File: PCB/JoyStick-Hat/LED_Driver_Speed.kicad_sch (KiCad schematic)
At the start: 0 parts

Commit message: Power and LED Driver
Power Supply Schematic sketched out using Pololu power regulator modules to hasten design. LED drivers replaced with ones that have 24 ouputs so we can use 20 unit bar graph LEDs and have 8 extra channels for other onboard LEDs
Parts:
- added J1: Conn_02x10_Counter_Clockwise, Connector_PinHeader_2.54mm:PinHeader_2x10_P2.54mm_Vertical, symbol Connector_Generic:Conn_02x10_Counter_Clockwise
- added U2: TLC5947DAP, AVR-KiCAD-Lib-ICs:DAP32_4P36X4P11, symbol AVR-KiCAD-Lib-ICs:TLC5947DAP
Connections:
- new net: J1.5 (Pin_5), U2.10 (OUT5)
- new net: J1.6 (Pin_6), U2.11 (OUT6)
- new net: J1.7 (Pin_7), U2.12 (OUT7)
- new net: J1.8 (Pin_8), U2.13 (OUT8)
- new net: J1.9 (Pin_9), U2.14 (OUT9)
- new net: J1.10 (Pin_10), U2.15 (OUT10)
- new net: J1.11 (Pin_11), U2.16 (OUT11)
- new net: J1.12 (Pin_12), U2.17 (OUT12)
- new net: J1.13 (Pin_13), U2.18 (OUT13)
- new net: J1.14 (Pin_14), U2.19 (OUT14)
- new net: J1.15 (Pin_15), U2.20 (OUT15)
- new net: J1.16 (Pin_16), U2.21 (OUT16)
- new net: J1.17 (Pin_17), U2.22 (OUT17)
- new net: J1.18 (Pin_18), U2.23 (OUT18)
- new net: J1.19 (Pin_19), U2.24 (OUT19)
- new net: J1.20 (Pin_20), U2.25 (OUT20)
- new net: J1.1 (Pin_1), U2.6 (OUT1)
- new net: J1.2 (Pin_2), U2.7 (OUT2)
- new net: J1.3 (Pin_3), U2.8 (OUT3)
- new net: J1.4 (Pin_4), U2.9 (OUT4)
- new net GND: U2.1 (GND), U2.33 (GND_PAD)

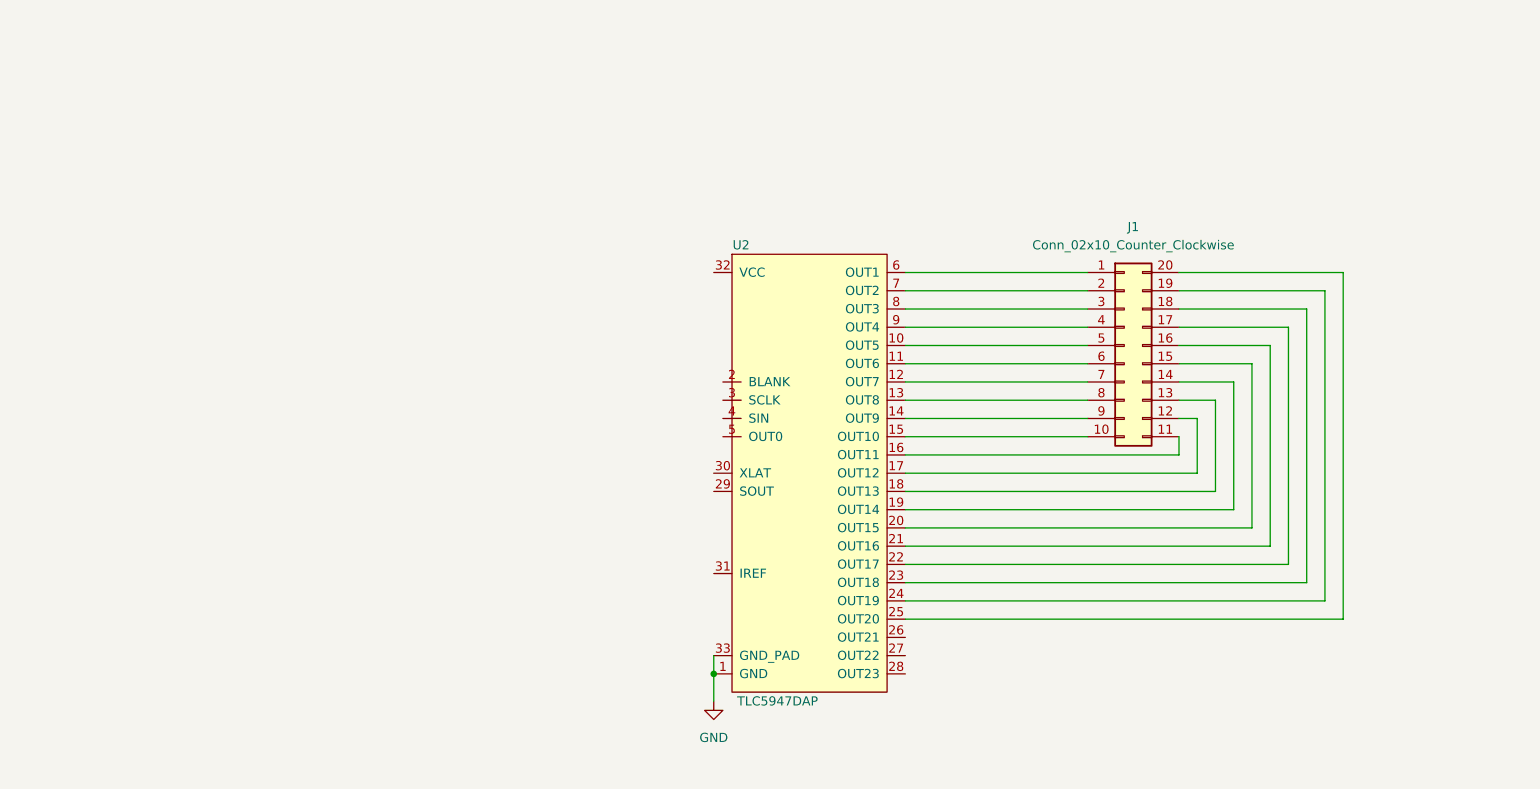
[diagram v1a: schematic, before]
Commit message: LED drivers and Joystick
Finished LED driver scheamtics, corrected some problems with symbols. added conenctors for joystick and buttons, connected RPI pins to MCU
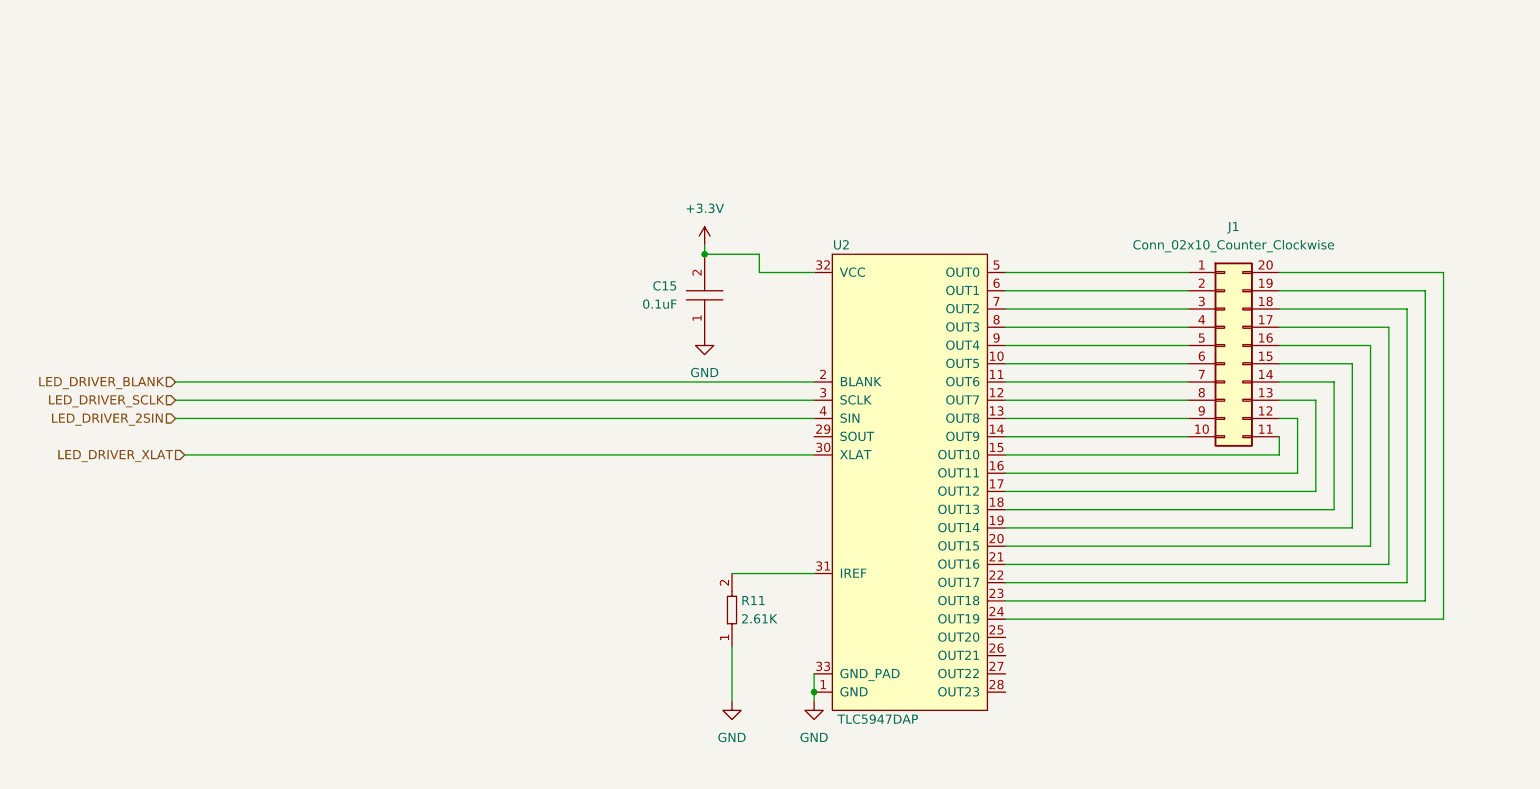
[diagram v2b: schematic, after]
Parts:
- added C15: CL10B104JB8NNNC, AVR-KiCAD-Lib-Capacitors:C0603, symbol AVR-KiCAD-Lib-Capacitors:CL10B104JB8NNNC
- added R11: RMCF0603FT2K61, AVR-KiCAD-Lib-Resistors:R0603, symbol AVR-KiCAD-Lib-Resistors:RMCF0603FT2K61
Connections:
- net GND: now also C15.1, R11.1
- net at U2.10 (OUT5): now also J1.6 (Pin_6); no longer J1.5 (Pin_5)
- net at U2.11 (OUT6): now also J1.7 (Pin_7); no longer J1.6 (Pin_6)
- net at U2.12 (OUT7): now also J1.8 (Pin_8); no longer J1.7 (Pin_7)
- net at U2.13 (OUT8): now also J1.9 (Pin_9); no longer J1.8 (Pin_8)
- net at U2.14 (OUT9): now also J1.10 (Pin_10); no longer J1.9 (Pin_9)
- net at U2.15 (OUT10): now also J1.11 (Pin_11); no longer J1.10 (Pin_10)
- net at U2.16 (OUT11): now also J1.12 (Pin_12); no longer J1.11 (Pin_11)
- net at U2.17 (OUT12): now also J1.13 (Pin_13); no longer J1.12 (Pin_12)
- net at U2.18 (OUT13): now also J1.14 (Pin_14); no longer J1.13 (Pin_13)
- net at U2.19 (OUT14): now also J1.15 (Pin_15); no longer J1.14 (Pin_14)
- net LED_DRIVER_BLANK: now reaches U2.2 (BLANK)
- net at U2.20 (OUT15): now also J1.16 (Pin_16); no longer J1.15 (Pin_15)
- net at U2.21 (OUT16): now also J1.17 (Pin_17); no longer J1.16 (Pin_16)
- net at U2.22 (OUT17): now also J1.18 (Pin_18); no longer J1.17 (Pin_17)
- net at U2.23 (OUT18): now also J1.19 (Pin_19); no longer J1.18 (Pin_18)
- net at U2.24 (OUT19): now also J1.20 (Pin_20); no longer J1.19 (Pin_19)
- net at U2.25 (OUT20): no longer J1.20 (Pin_20)
- net LED_DRIVER_SCLK: now reaches U2.3 (SCLK)
- net LED_DRIVER_XLAT: now reaches U2.30 (XLAT)
- net at U2.31 (IREF): now also R11.2
- net +3.3V: now reaches U2.32 (VCC)
- net +3.3V: now also C15.2
- net LED_DRIVER_2SIN: now reaches U2.4 (SIN)
- net at U2.5 (OUT0): now also J1.1 (Pin_1)
- net at U2.6 (OUT1): now also J1.2 (Pin_2); no longer J1.1 (Pin_1)
- net at U2.7 (OUT2): now also J1.3 (Pin_3); no longer J1.2 (Pin_2)
- net at U2.8 (OUT3): now also J1.4 (Pin_4); no longer J1.3 (Pin_3)
- net at U2.9 (OUT4): now also J1.5 (Pin_5); no longer J1.4 (Pin_4)
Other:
- moved on the sheet: J1, U2

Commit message: Schematic Progress
Made progress with schematic and corrected designator letters with connectors to match the built in paradigm of using J instead of T. T will not be used to referencing transformers instead of connectors.
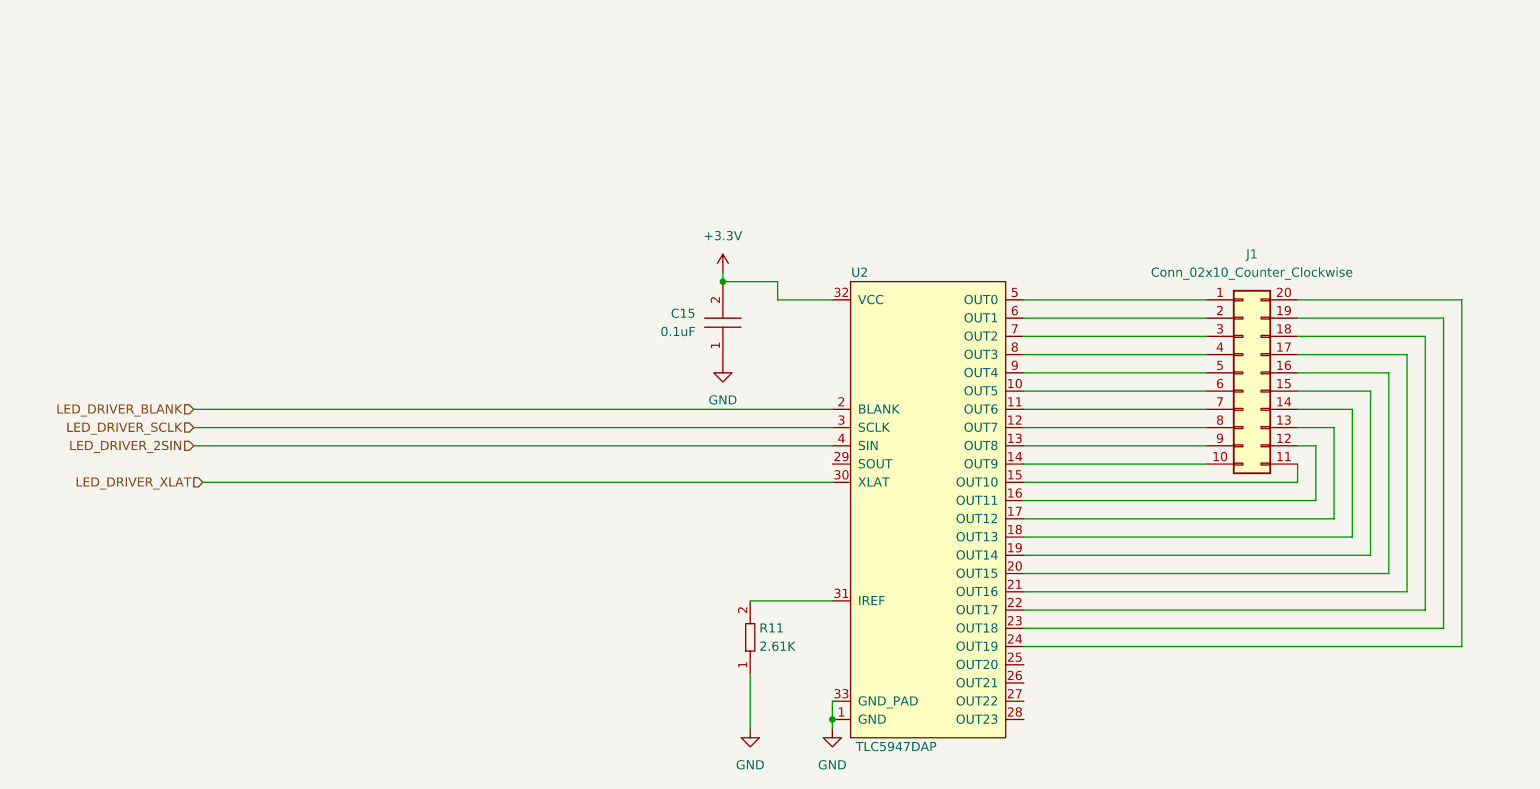
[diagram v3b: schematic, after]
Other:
- moved on the sheet: C15, J1, R11, U2

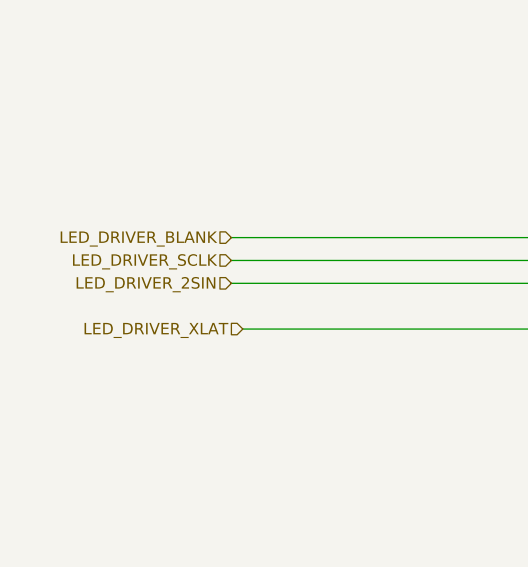
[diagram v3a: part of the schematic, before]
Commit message: Schematic Complete
Schematic completed. Moved to 100 pin version of STM32 MCU for more connectivity and better muxing of internal peripherals with pins.
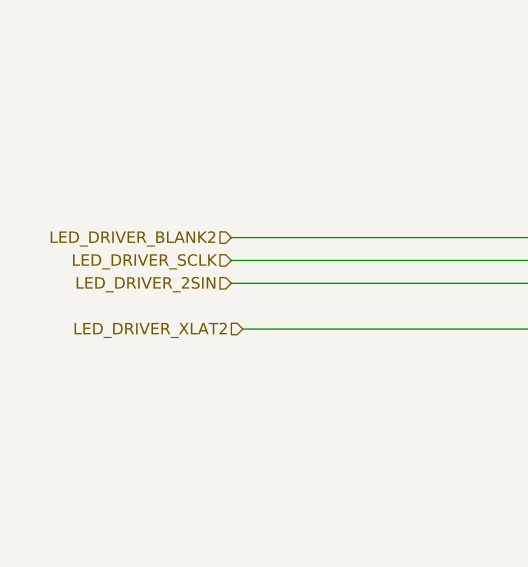
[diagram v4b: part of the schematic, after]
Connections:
- net LED_DRIVER_BLANK renamed LED_DRIVER_BLANK2
- net LED_DRIVER_XLAT renamed LED_DRIVER_XLAT2
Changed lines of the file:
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@@
     (stroke (width 0) (type default))
   )
-  (hierarchical_label "LED_DRIVER_XLAT" (shape input) (at 36.83 91.44 180) (fields_autoplaced)
+  (hierarchical_label "LED_DRIVER_XLAT2" (shape input) (at 36.83 91.44 180) (fields_autoplaced)
     (effects (font (size 1.27 1.27)) (justify right))
   )
@@
     (effects (font (size 1.27 1.27)) (justify right))
   )
-  (hierarchical_label "LED_DRIVER_BLANK" (shape input) (at 35.56 81.28 180) (fields_autoplaced)
+  (hierarchical_label "LED_DRIVER_BLANK2" (shape input) (at 35.56 81.28 180) (fields_autoplaced)
     (effects (font (size 1.27 1.27)) (justify right))
   )

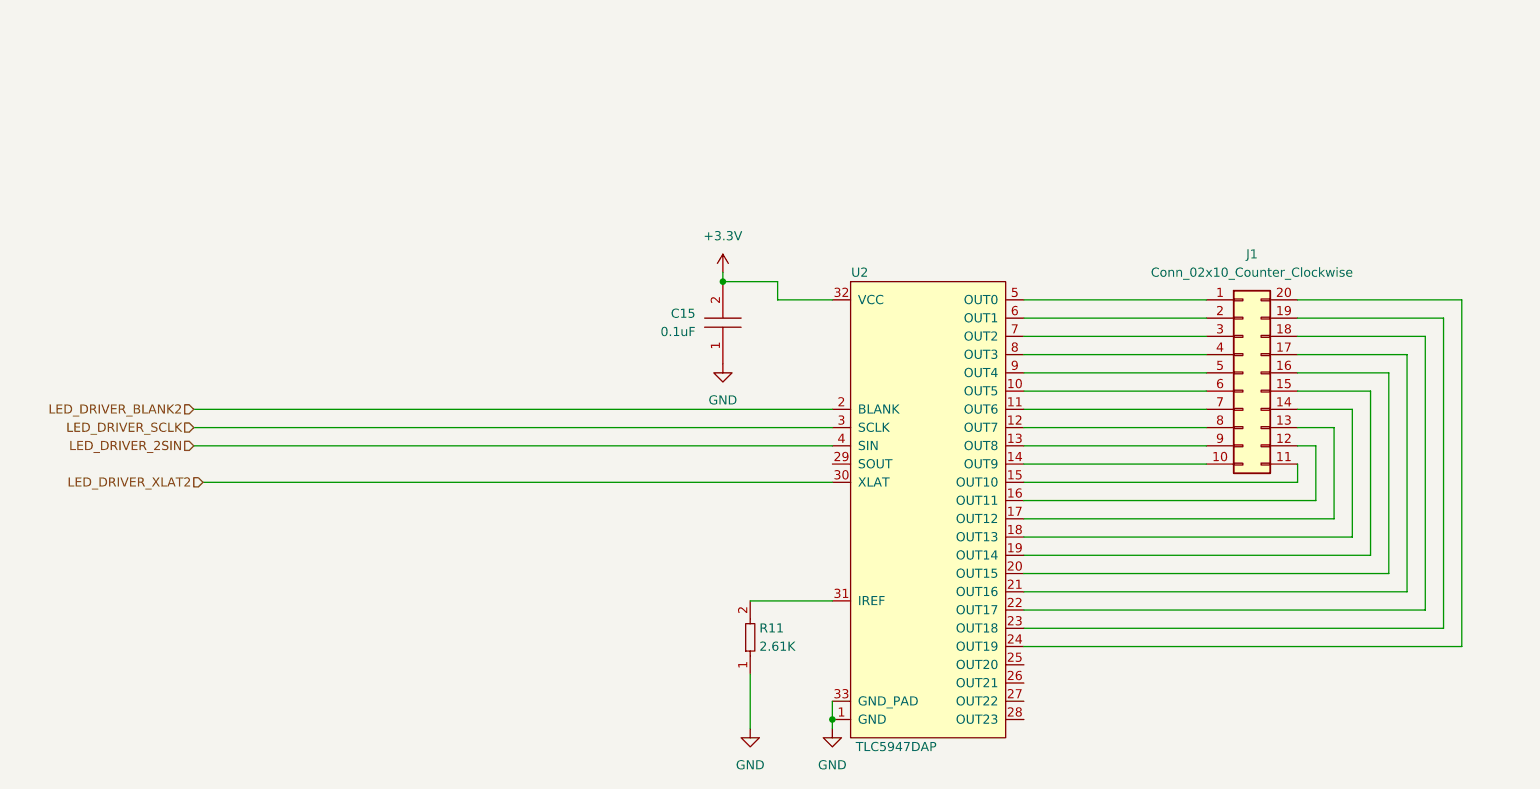
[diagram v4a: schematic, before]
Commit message: LEDs and Additional connectors
Added heartbeat and diagnostic LEDs to STM32 and RPi3 schematics so we can directly flash them for debug purposes. Added a connector for serial port diagnostics on STM32. Added rotary switch interface for STM32 and added pullups to button connectors.
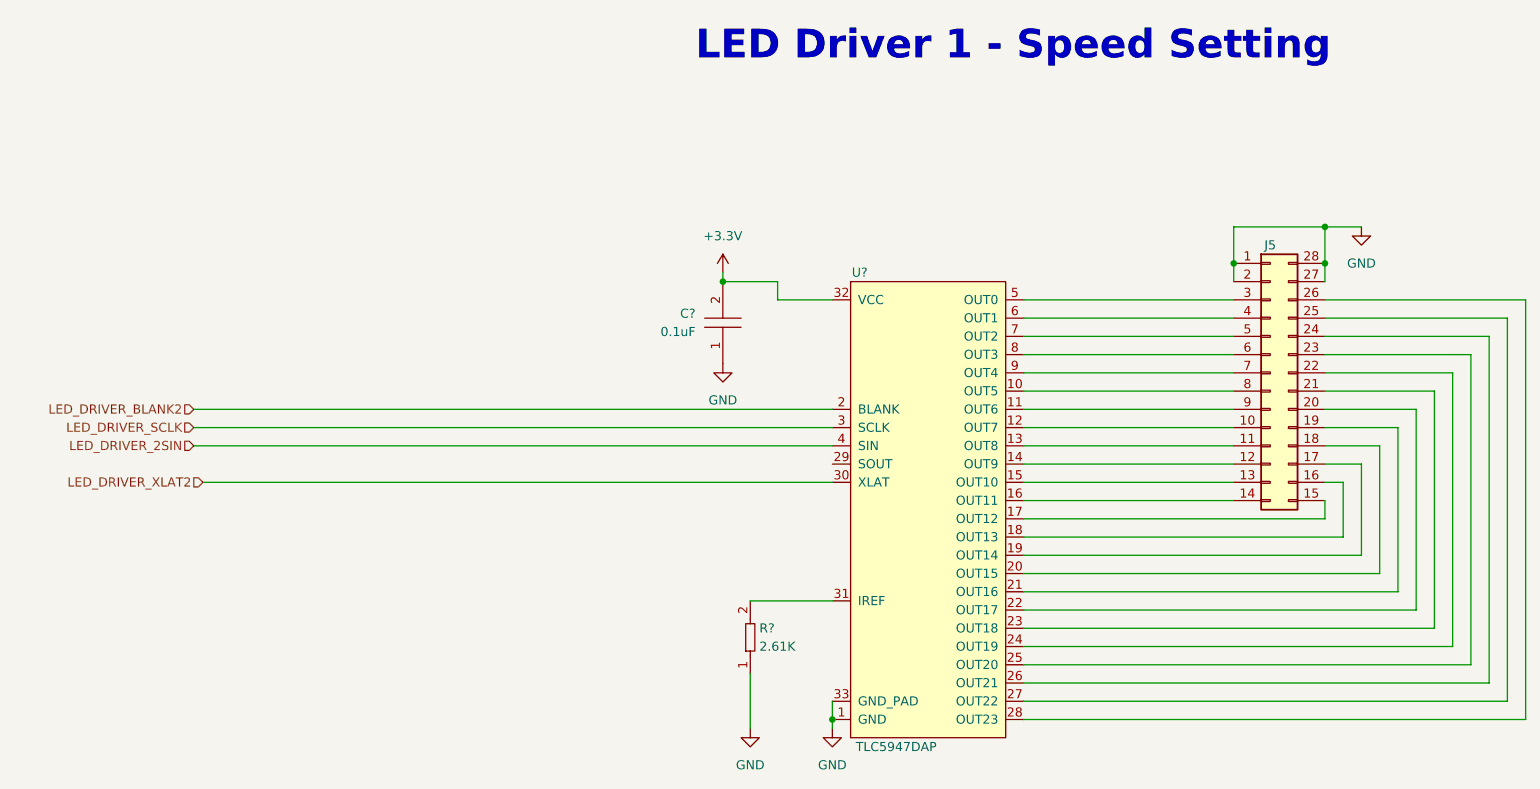
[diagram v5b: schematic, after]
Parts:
- removed J1: Conn_02x10_Counter_Clockwise, Connector_PinHeader_2.54mm:PinHeader_2x10_P2.54mm_Vertical, symbol Connector_Generic:Conn_02x10_Counter_Clockwise
- added J5: Conn_02x14_Counter_Clockwise, Connector_PinHeader_2.54mm:PinHeader_2x14_P2.54mm_Vertical, symbol Connector_Generic:Conn_02x14_Counter_Clockwise
- renumbered C15 to C?, R11 to R?, U2 to U?
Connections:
- net GND: now also J5.1 (Pin_1), J5.2 (Pin_2), J5.27 (Pin_27), J5.28 (Pin_28)
- net at U?.10 (OUT5): now also J5.8 (Pin_8)
- net at U?.11 (OUT6): now also J5.9 (Pin_9)
- net at U?.12 (OUT7): now also J5.10 (Pin_10)
- net at U?.13 (OUT8): now also J5.11 (Pin_11)
- net at U?.14 (OUT9): now also J5.12 (Pin_12)
- net at U?.15 (OUT10): now also J5.13 (Pin_13)
- net at U?.16 (OUT11): now also J5.14 (Pin_14)
- net at U?.17 (OUT12): now also J5.15 (Pin_15)
- net at U?.18 (OUT13): now also J5.16 (Pin_16)
- net at U?.19 (OUT14): now also J5.17 (Pin_17)
- net at U?.20 (OUT15): now also J5.18 (Pin_18)
- net at U?.21 (OUT16): now also J5.19 (Pin_19)
- net at U?.22 (OUT17): now also J5.20 (Pin_20)
- net at U?.23 (OUT18): now also J5.21 (Pin_21)
- net at U?.24 (OUT19): now also J5.22 (Pin_22)
- net at U?.25 (OUT20): now also J5.23 (Pin_23)
- net at U?.26 (OUT21): now also J5.24 (Pin_24)
- net at U?.27 (OUT22): now also J5.25 (Pin_25)
- net at U?.28 (OUT23): now also J5.26 (Pin_26)
- net at U?.5 (OUT0): now also J5.3 (Pin_3)
- net at U?.6 (OUT1): now also J5.4 (Pin_4)
- net at U?.7 (OUT2): now also J5.5 (Pin_5)
- net at U?.8 (OUT3): now also J5.6 (Pin_6)
- net at U?.9 (OUT4): now also J5.7 (Pin_7)
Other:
- note added: "LED Driver 1 - Speed Setting"
